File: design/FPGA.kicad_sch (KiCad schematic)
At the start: 16 parts

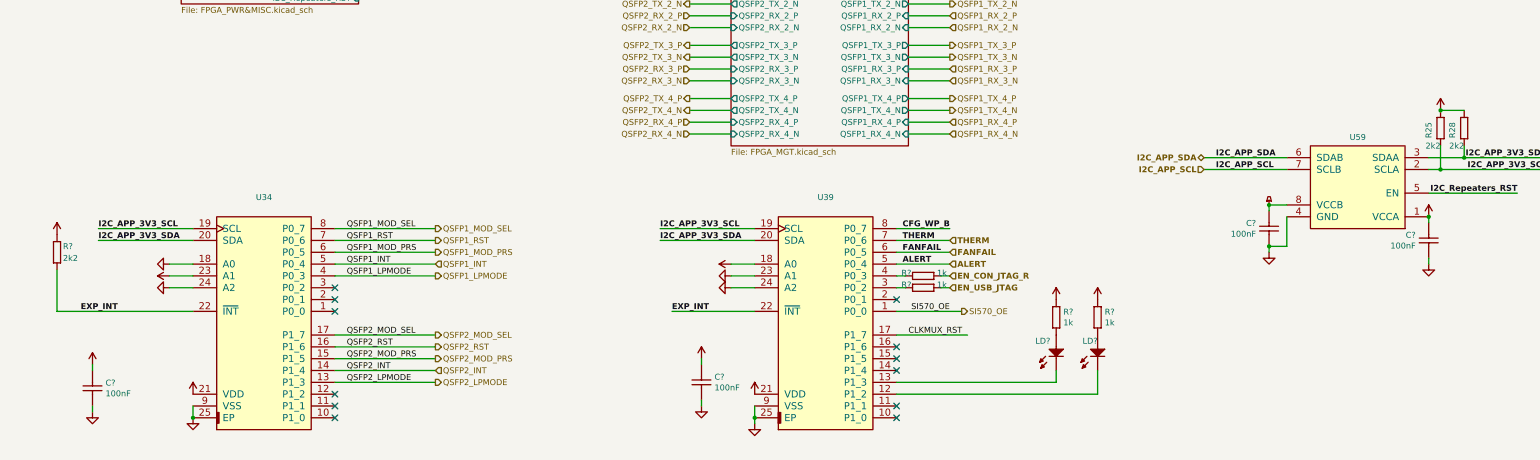
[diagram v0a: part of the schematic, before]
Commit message: new power converter added
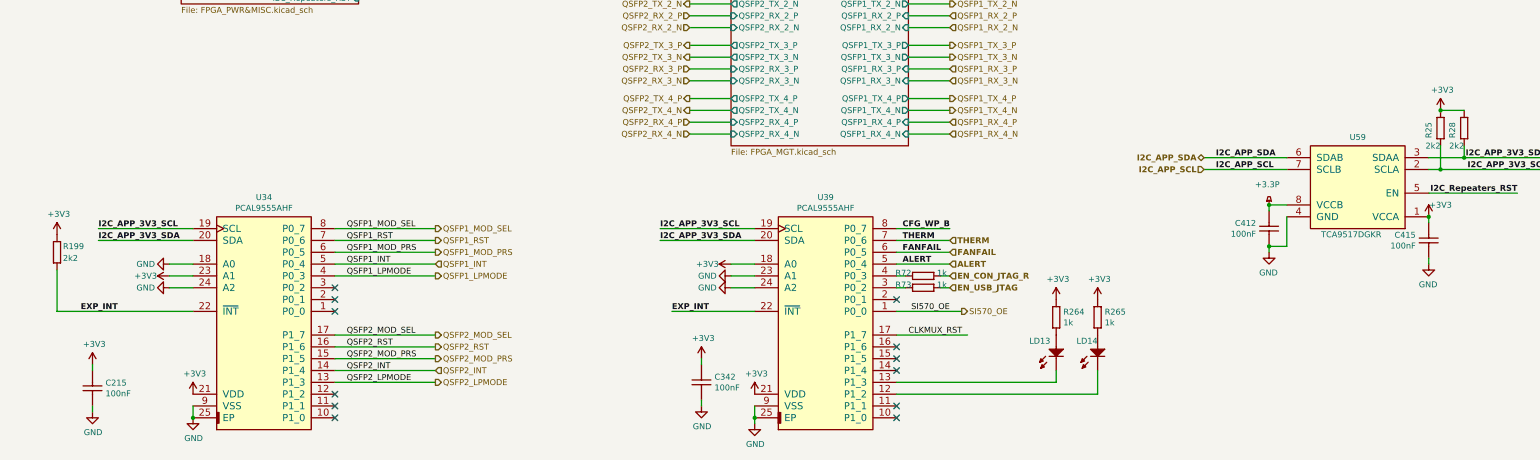
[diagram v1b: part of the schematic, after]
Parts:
- C215, C342, C412, C415: renamed from C?; value (none) -> CC0201_100NF_6.3V_10%_X5R; footprint (none) -> CAPC0603X33N
- LD13, LD14: renamed from LD?; value (none) -> LED_KINGBRIGHT_KPH-1608CGCK; footprint (none) -> ICs And Semiconductors SMD:LED_KINGBRIGHT_KPH-1608CGCK
- R199: renamed from R?; value (none) -> R0402_2K2_1%_0.0625W_100PPM; footprint (none) -> RESC1005X40N
- R25, R28: value (none) -> R0402_2K2_1%_0.0625W_100PPM; footprint (none) -> RESC1005X40N
- R264, R265, R72, R73: renamed from R?; value (none) -> R0402_1K_1%_0.0625W_100PPM; footprint (none) -> RESC1005X40N
- U34, U39: value (none) -> PCAL9555AHF; footprint (none) -> ICs And Semiconductors SMD:QFN50P400X400X80-25N-S225
- U59: value (none) -> TCA9517DGKR; footprint (none) -> ICs And Semiconductors SMD:SOP65P490X110-8N

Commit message: connected signals to the J9 connector
connected signals to the J9 connector
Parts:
- C215, C342, C412, C415, R199, R25, R264, R265, R28, R72, R73: Author CERN DEM JLC -> (none)
- LD13, LD14: Author CERN DEM JLC -> (none); Bonding No -> (none); Color Green -> (none)
- U34, U39: Author CERN DEM BC -> (none); Bonding No -> (none)
- U59: Author CERN DEM JLC -> (none); Bonding No -> (none)
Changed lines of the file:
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@@
       (effects (font (size 1.524 1.524)) (justify left) hide)
     )
-    (property "Bonding" "No" (id 24) (at 187.96 330.2 0)
+    (property "Bonding" "" (id 24) (at 187.96 330.2 0)
       (effects (font (size 1.524 1.524)) (justify left) hide)
     )
@@
       (effects (font (size 1.524 1.524)) (justify left) hide)
     )
-    (property "Author" "CERN DEM BC" (id 29) (at 187.96 341.63 0)
+    (property "Author" "" (id 29) (at 187.96 341.63 0)
       (effects (font (size 1.524 1.524)) (justify left) hide)
     )
@@
       (effects (font (size 1.524 1.524)) (justify left) hide)
     )
-    (property "Bonding" "No" (id 24) (at 67.31 330.2 0)
+    (property "Bonding" "" (id 24) (at 67.31 330.2 0)
       (effects (font (size 1.524 1.524)) (justify left) hide)
     )
@@
       (effects (font (size 1.524 1.524)) (justify left) hide)
     )
-    (property "Author" "CERN DEM BC" (id 29) (at 67.31 341.63 0)
+    (property "Author" "" (id 29) (at 67.31 341.63 0)
       (effects (font (size 1.524 1.524)) (justify left) hide)
     )
@@
       (effects (font (size 1.524 1.524)) (justify left) hide)
     )
-    (property "Author" "CERN DEM JLC" (id 35) (at -45.974 257.81 0)
+    (property "Author" "" (id 35) (at -45.974 257.81 0)
       (effects (font (size 1.524 1.524)) (justify left) hide)
     )
@@
       (effects (font (size 1.524 1.524)) (justify left) hide)
     )
-    (property "Author" "CERN DEM JLC" (id 35) (at 84.836 256.54 0)
+    (property "Author" "" (id 35) (at 84.836 256.54 0)
       (effects (font (size 1.524 1.524)) (justify left) hide)
     )
@@
       (effects (font (size 1.524 1.524)) (justify left) hide)
     )
-    (property "Author" "CERN DEM JLC" (id 36) (at -54.61 228.6 0)
+    (property "Author" "" (id 36) (at -54.61 228.6 0)
       (effects (font (size 1.524 1.524)) (justify left) hide)
     )
@@
       (effects (font (size 1.524 1.524)) (justify left) hide)
     )
-    (property "Author" "CERN DEM JLC" (id 36) (at 168.91 242.57 0)
+    (property "Author" "" (id 36) (at 168.91 242.57 0)
       (effects (font (size 1.524 1.524)) (justify left) hide)
     )
@@
       (effects (font (size 1.524 1.524)) (justify left) hide)
     )
-    (property "Author" "CERN DEM JLC" (id 36) (at 160.02 242.57 0)
+    (property "Author" "" (id 36) (at 160.02 242.57 0)
       (effects (font (size 1.524 1.524)) (justify left) hide)
     )
@@
       (effects (font (size 1.524 1.524)) (justify left) hide)
     )
-    (property "Color" "Green" (id 10) (at 274.066 254 0)
+    (property "Color" "" (id 10) (at 274.066 254 0)
       (effects (font (size 1.524 1.524)) (justify left) hide)
     )
@@
       (effects (font (size 1.524 1.524)) (justify left) hide)
     )
-    (property "Bonding" "No" (id 25) (at 310.642 254 0)
+    (property "Bonding" "" (id 25) (at 310.642 254 0)
       (effects (font (size 1.524 1.524)) (justify left) hide)
     )
@@
       (effects (font (size 1.524 1.524)) (justify left) hide)
     )
-    (property "Author" "CERN DEM JLC" (id 32) (at 333.502 254 0)
+    (property "Author" "" (id 32) (at 333.502 254 0)
       (effects (font (size 1.524 1.524)) (justify left) hide)
     )
@@
       (effects (font (size 1.524 1.524)) (justify left) hide)
     )
-    (property "Color" "Green" (id 10) (at 282.956 254 0)
+    (property "Color" "" (id 10) (at 282.956 254 0)
       (effects (font (size 1.524 1.524)) (justify left) hide)
     )
@@
       (effects (font (size 1.524 1.524)) (justify left) hide)
     )
-    (property "Bonding" "No" (id 25) (at 319.532 254 0)
+    (property "Bonding" "" (id 25) (at 319.532 254 0)
       (effects (font (size 1.524 1.524)) (justify left) hide)
     )
@@
       (effects (font (size 1.524 1.524)) (justify left) hide)
     )
-    (property "Author" "CERN DEM JLC" (id 32) (at 342.392 254 0)
+    (property "Author" "" (id 32) (at 342.392 254 0)
       (effects (font (size 1.524 1.524)) (justify left) hide)
     )
@@
       (effects (font (size 1.27 1.27)) (justify left) hide)
     )
-    (property "Bonding" "No" (id 24) (at 322.58 275.59 0)
+    (property "Bonding" "" (id 24) (at 322.58 275.59 0)
       (effects (font (size 1.27 1.27)) (justify left) hide)
     )
@@
       (effects (font (size 1.27 1.27)) (justify left) hide)
     )
-    (property "Author" "CERN DEM JLC" (id 29) (at 322.58 285.115 0)
+    (property "Author" "" (id 29) (at 322.58 285.115 0)
       (effects (font (size 1.27 1.27)) (justify left) hide)
     )
@@
       (effects (font (size 1.524 1.524)) (justify left) hide)
     )
-    (property "Author" "CERN DEM JLC" (id 35) (at 414.274 226.06 0)
+    (property "Author" "" (id 35) (at 414.274 226.06 0)
       (effects (font (size 1.524 1.524)) (justify left) hide)
     )
@@
       (effects (font (size 1.524 1.524)) (justify left) hide)
     )
-    (property "Author" "CERN DEM JLC" (id 35) (at 379.984 223.52 0)
+    (property "Author" "" (id 35) (at 379.984 223.52 0)
       (effects (font (size 1.524 1.524)) (justify left) hide)
     )
@@
       (effects (font (size 1.524 1.524)) (justify left) hide)
     )
-    (property "Author" "CERN DEM JLC" (id 36) (at 422.91 201.93 0)
+    (property "Author" "" (id 36) (at 422.91 201.93 0)
       (effects (font (size 1.524 1.524)) (justify left) hide)
     )
@@
       (effects (font (size 1.524 1.524)) (justify left) hide)
     )
-    (property "Author" "CERN DEM JLC" (id 36) (at 417.83 201.93 0)
+    (property "Author" "" (id 36) (at 417.83 201.93 0)
       (effects (font (size 1.524 1.524)) (justify left) hide)
     )
@@
       (effects (font (size 1.524 1.524)) (justify left) hide)
     )
-    (property "Author" "CERN DEM JLC" (id 36) (at 222.885 149.86 0)
+    (property "Author" "" (id 36) (at 222.885 149.86 0)
       (effects (font (size 1.524 1.524)) (justify left) hide)
     )
@@
       (effects (font (size 1.524 1.524)) (justify left) hide)
     )
-    (property "Author" "CERN DEM JLC" (id 36) (at 222.885 152.4 0)
-      (effects (font (size 1.524 1.524)) (justify left) hide)
-    )
+    (property "Author" "" (id 36) (at 222.885 152.4 0)
+      (effects (font (size 1.524 1.524)) (justify left) hide)
+    )

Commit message: external clock connected to power supply IC, PCB routing
external clock connected to power supply IC, PCB routing
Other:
- sheet FPGA_14_15 ports: added none; removed FPGA_XR_GPIO_0
- sheet FPGA_32_16 ports: added FPGA_CLKIN0, FPGA_CLKIN12, FPGA_CLKIN3; removed none
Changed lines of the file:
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@@
     (stroke (width 0) (type default) (color 0 0 0 0))
   )
+  (wire (pts (xy 203.2 67.31) (xy 213.36 67.31))
+    (stroke (width 0) (type default) (color 0 0 0 0))
+  )
   (wire (pts (xy 168.91 207.01) (xy 177.8 207.01))
     (stroke (width 0) (type default) (color 0 0 0 0))
@@
     (stroke (width 0) (type default) (color 0 0 0 0))
   )
+  (wire (pts (xy 203.2 64.77) (xy 213.36 64.77))
+    (stroke (width 0) (type default) (color 0 0 0 0))
+  )
   (wire (pts (xy 92.71 232.41) (xy 114.3 232.41))
     (stroke (width 0) (type default) (color 0 0 0 0))
@@
     (stroke (width 0) (type default) (color 0 0 0 0))
   )
+  (wire (pts (xy 203.2 69.85) (xy 213.36 69.85))
+    (stroke (width 0) (type default) (color 0 0 0 0))
+  )
   (wire (pts (xy 215.9 165.1) (xy 224.79 165.1))
     (stroke (width 0) (type default) (color 0 0 0 0))
@@
     (stroke (width 0) (type default) (color 0 0 0 0))
   )
-  (wire (pts (xy 290.83 57.15) (xy 294.64 57.15))
-    (stroke (width 0) (type default) (color 0 0 0 0))
-  )
   (wire (pts (xy 106.68 147.32) (xy 97.79 147.32))
     (stroke (width 0) (type default) (color 0 0 0 0))
@@
     (effects (font (size 1.27 1.27)) (justify right))
   )
+  (hierarchical_label "FPGA_CLKIN0" (shape output) (at 213.36 64.77 0)
+    (effects (font (size 1.27 1.27) (thickness 0.254) bold) (justify left))
+  )
   (hierarchical_label "VCXO_EN" (shape input) (at 110.49 90.17 0)
     (effects (font (size 1.27 1.27) (thickness 0.254) bold) (justify left))
@@
     (effects (font (size 1.27 1.27)) (justify right))
   )
-  (hierarchical_label "FPGA_XR_GPIO_0" (shape output) (at 294.64 57.15 0)
-    (effects (font (size 1.27 1.27) (thickness 0.254) bold) (justify left))
-  )
   (hierarchical_label "QSFP2_TX_4_N" (shape output) (at 168.91 201.93 180)
     (effects (font (size 1.27 1.27)) (justify right))
@@
     (effects (font (size 1.27 1.27) (thickness 0.254) bold) (justify left))
   )
+  (hierarchical_label "FPGA_CLKIN3" (shape output) (at 213.36 69.85 0)
+    (effects (font (size 1.27 1.27) (thickness 0.254) bold) (justify left))
+  )
   (hierarchical_label "QSFP2_RX_2_N" (shape input) (at 168.91 184.15 180)
     (effects (font (size 1.27 1.27)) (justify right))
@@
     (effects (font (size 1.27 1.27) (thickness 0.254) bold) (justify right))
   )
+  (hierarchical_label "FPGA_CLKIN12" (shape output) (at 213.36 67.31 0)
+    (effects (font (size 1.27 1.27) (thickness 0.254) bold) (justify left))
+  )
   (hierarchical_label "DDR3_DQS2_N" (shape bidirectional) (at 147.32 66.04 180)
     (effects (font (size 1.27 1.27)) (justify right))
@@
       (effects (font (size 1.27 1.27)) (justify right))
     )
+    (pin "FPGA_CLKIN0" output (at 203.2 64.77 0)
+      (effects (font (size 1.27 1.27)) (justify right))
+    )
+    (pin "FPGA_CLKIN12" output (at 203.2 67.31 0)
+      (effects (font (size 1.27 1.27)) (justify right))
+    )
+    (pin "FPGA_CLKIN3" output (at 203.2 69.85 0)
+      (effects (font (size 1.27 1.27)) (justify right))
+    )
   )
   (sheet (at 252.73 43.18) (size 38.1 60.96) (fields_autoplaced)
@@
       (effects (font (size 1.27 1.27)) (justify right))
     )
-    (pin "FPGA_XR_GPIO_0" output (at 290.83 57.15 0)
-      (effects (font (size 1.27 1.27)) (justify right))
-    )
